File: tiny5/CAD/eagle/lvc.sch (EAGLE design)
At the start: 6 parts, among them U1 LT3007

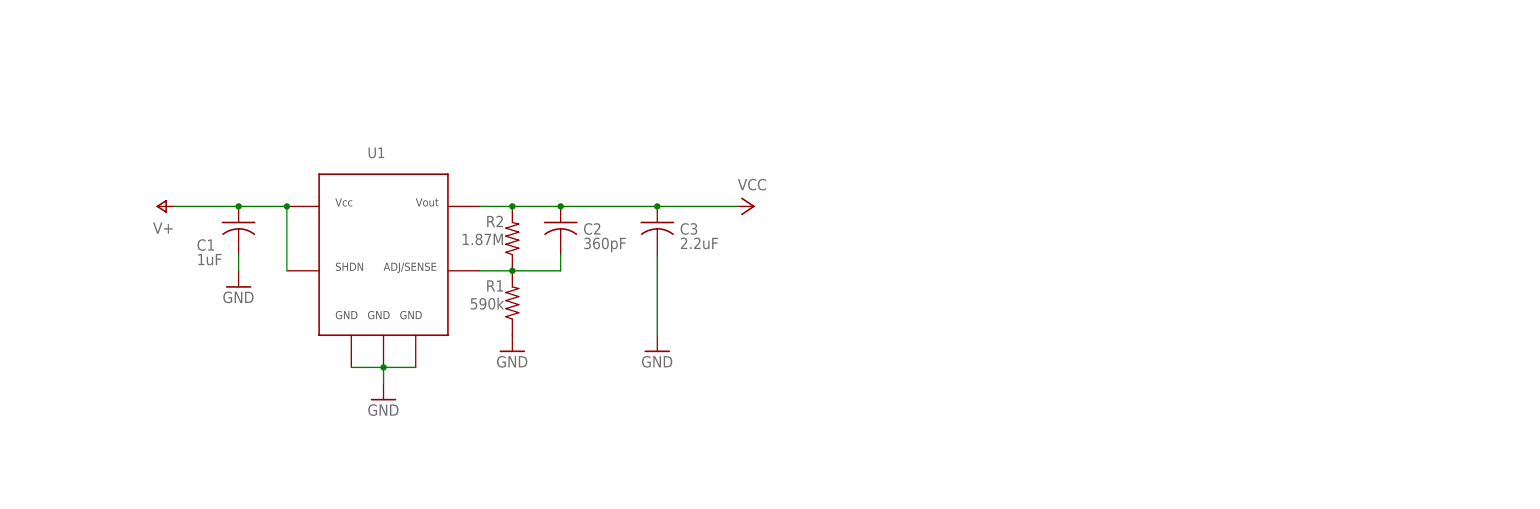
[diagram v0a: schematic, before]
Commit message: added mcu block, updated libraries
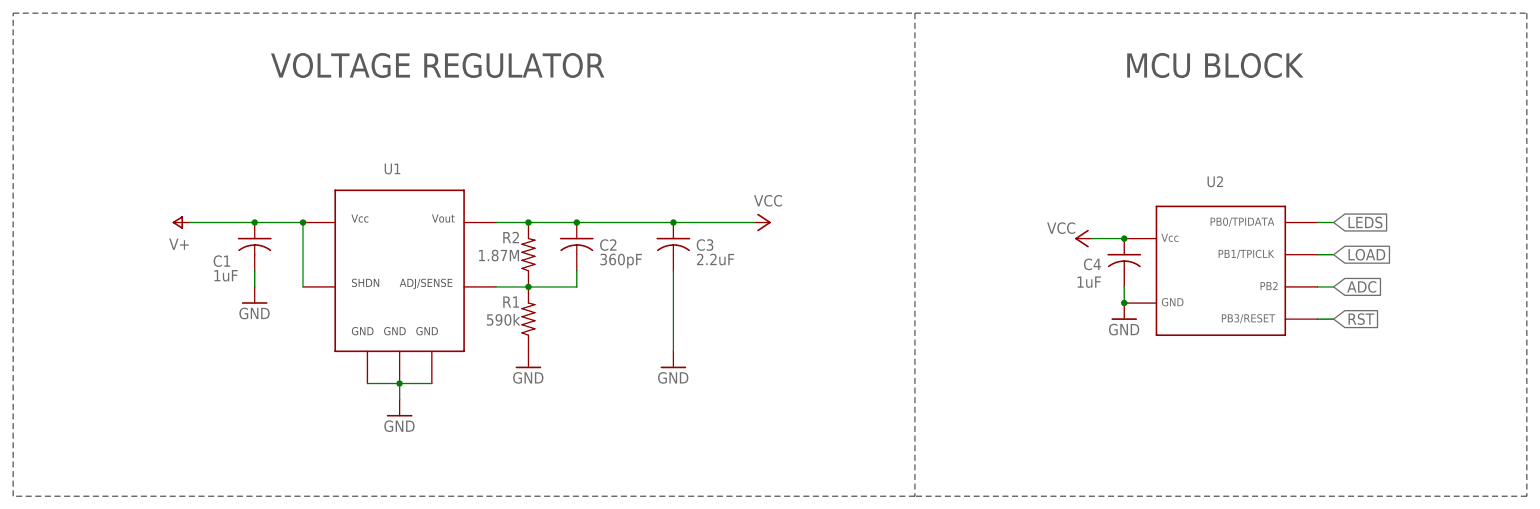
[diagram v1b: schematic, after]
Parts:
- added C4: 1uF, resistor:C-USC0603
- added U2: ATTINY5, AR_mcu:ATTINY5
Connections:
- new net ADC: U2.PB2
- new net LEDS: U2.PB0/TPID
- new net LOAD: U2.PB1/TPICLK
- new net RST: U2.PB3/RST
- net GND: now also C4.2, U2.GND
- net VCC: now also C4.1, U2.VCC
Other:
- note added: "MCU BLOCK"
- note added: "VOLTAGE REGULATOR"
- moved on the sheet: C1, C2, C3, R1, R2, U1

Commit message: Went from adjustable to fixed voltage reg.
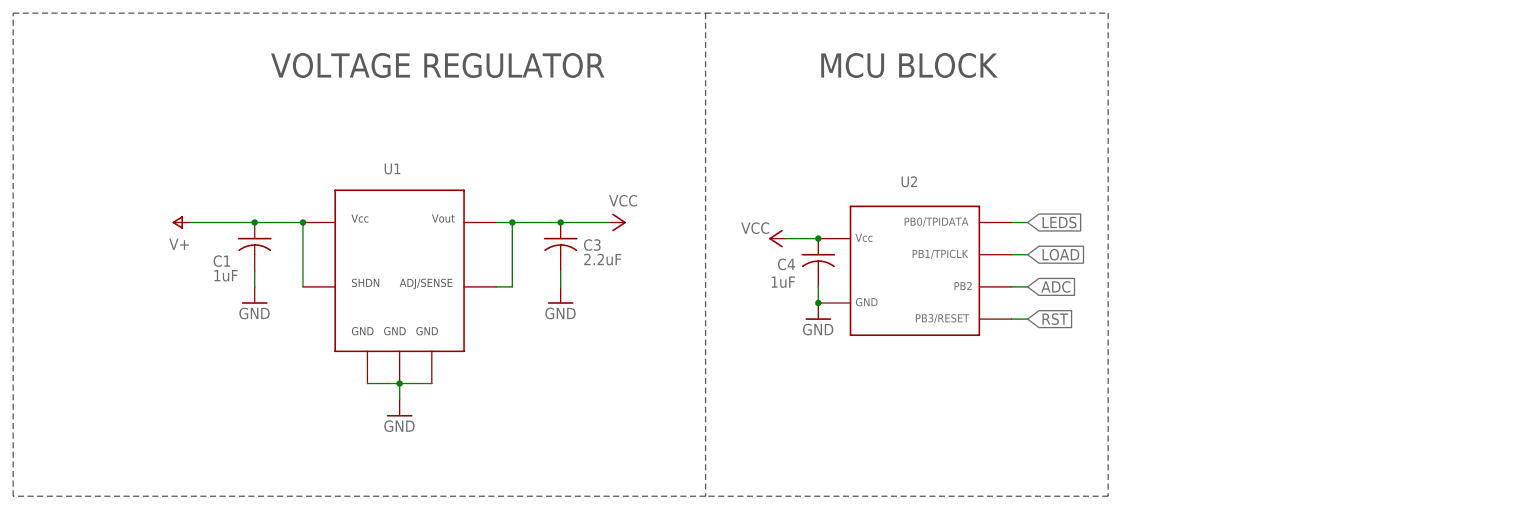
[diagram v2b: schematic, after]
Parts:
- removed C2: 360pF, resistor:C-USC0603
- removed R1: 590k, resistor:R-US_R0603
- removed R2: 1.87M, resistor:R-US_R0603
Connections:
- removed net N$2: C2.2, R1.2, R2.1, U1.ADJ/SENSE
- net GND: no longer R1.1
- net VCC: now also U1.ADJ/SENSE; no longer C2.1, R2.2
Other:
- moved on the sheet: C3, C4, U2
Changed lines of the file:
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@@
 <part name="C1" library="resistor" deviceset="C-US" device="C0603" value="1uF"/>
 <part name="GND2" library="supply1" deviceset="GND" device=""/>
-<part name="R1" library="resistor" deviceset="R-US_" device="R0603" value="590k"/>
-<part name="R2" library="resistor" deviceset="R-US_" device="R0603" value="1.87M"/>
-<part name="GND3" library="supply1" deviceset="GND" device=""/>
 <part name="U1" library="AR_voltage_reg" deviceset="LT3007" device=""/>
-<part name="C2" library="resistor" deviceset="C-US" device="C0603" value="360pF"/>
 <part name="C3" library="resistor" deviceset="C-US" device="C0603" value="2.2uF"/>
 <part name="GND4" library="supply1" deviceset="GND" device=""/>
@@
 <sheet>
 <plain>
-<wire x1="-71.12" y1="99.06" x2="25.4" y2="99.06" width="0.1524" layer="97" style="shortdash"/>
-<wire x1="25.4" y1="99.06" x2="25.4" y2="22.86" width="0.1524" layer="97" style="shortdash"/>
-<wire x1="25.4" y1="22.86" x2="-71.12" y2="22.86" width="0.1524" layer="97" style="shortdash"/>
-<wire x1="-71.12" y1="22.86" x2="-213.36" y2="22.86" width="0.1524" layer="97" style="shortdash"/>
+<wire x1="-104.14" y1="99.06" x2="-40.64" y2="99.06" width="0.1524" layer="97" style="shortdash"/>
+<wire x1="-40.64" y1="99.06" x2="-40.64" y2="22.86" width="0.1524" layer="97" style="shortdash"/>
+<wire x1="-40.64" y1="22.86" x2="-104.14" y2="22.86" width="0.1524" layer="97" style="shortdash"/>
+<wire x1="-104.14" y1="22.86" x2="-213.36" y2="22.86" width="0.1524" layer="97" style="shortdash"/>
 <wire x1="-213.36" y1="22.86" x2="-213.36" y2="99.06" width="0.1524" layer="97" style="shortdash"/>
-<wire x1="-213.36" y1="99.06" x2="-71.12" y2="99.06" width="0.1524" layer="97" style="shortdash"/>
-<wire x1="-71.12" y1="99.06" x2="-71.12" y2="22.86" width="0.1524" layer="97" style="shortdash"/>
+<wire x1="-213.36" y1="99.06" x2="-104.14" y2="99.06" width="0.1524" layer="97" style="shortdash"/>
+<wire x1="-104.14" y1="99.06" x2="-104.14" y2="22.86" width="0.1524" layer="97" style="shortdash"/>
 <text x="-172.72" y="88.9" size="3.81" layer="97">VOLTAGE REGULATOR</text>
-<text x="-38.1" y="88.9" size="3.81" layer="97">MCU BLOCK</text>
+<text x="-86.36" y="88.9" size="3.81" layer="97">MCU BLOCK</text>
 </plain>
 <instances>
@@
 </instance>
 <instance part="GND2" gate="1" x="-175.26" y="53.34"/>
-<instance part="R1" gate="G$1" x="-132.08" y="50.8" smashed="yes" rot="R90">
-<attribute name="NAME" x="-133.35" y="54.3814" size="1.778" layer="95" rot="R180"/>
-<attribute name="VALUE" x="-133.35" y="51.562" size="1.778" layer="96" rot="R180"/>
-</instance>
-<instance part="R2" gate="G$1" x="-132.08" y="60.96" smashed="yes" rot="R90">
-<attribute name="NAME" x="-133.35" y="64.5414" size="1.778" layer="95" rot="R180"/>
-<attribute name="VALUE" x="-133.35" y="61.722" size="1.778" layer="96" rot="R180"/>
-</instance>
-<instance part="GND3" gate="1" x="-132.08" y="43.18"/>
 <instance part="U1" gate="G$1" x="-152.4" y="58.42" smashed="yes">
 <attribute name="NAME" x="-154.94" y="73.66" size="1.6764" layer="95"/>
 </instance>
-<instance part="C2" gate="G$1" x="-124.46" y="63.5" smashed="yes">
-<attribute name="NAME" x="-120.904" y="61.595" size="1.778" layer="95"/>
-<attribute name="VALUE" x="-120.904" y="59.309" size="1.778" layer="96"/>
+<instance part="C3" gate="G$1" x="-127" y="63.5" smashed="yes">
+<attribute name="NAME" x="-123.444" y="61.595" size="1.778" layer="95"/>
+<attribute name="VALUE" x="-123.444" y="59.309" size="1.778" layer="96"/>
 </instance>
-<instance part="C3" gate="G$1" x="-109.22" y="63.5" smashed="yes">
-<attribute name="NAME" x="-105.664" y="61.595" size="1.778" layer="95"/>
-<attribute name="VALUE" x="-105.664" y="59.309" size="1.778" layer="96"/>
+<instance part="GND4" gate="1" x="-127" y="53.34"/>
+<instance part="P+1" gate="VCC" x="-116.84" y="66.04" rot="R270"/>
+<instance part="P+2" gate="1" x="-187.96" y="66.04" rot="R90"/>
+<instance part="P+3" gate="VCC" x="-93.98" y="63.5" smashed="yes" rot="R90">
+<attribute name="VALUE" x="-93.98" y="66.04" size="1.778" layer="96" rot="R180"/>
 </instance>
-<instance part="GND4" gate="1" x="-109.22" y="43.18"/>
-<instance part="P+1" gate="VCC" x="-93.98" y="66.04" rot="R270"/>
-<instance part="P+2" gate="1" x="-187.96" y="66.04" rot="R90"/>
-<instance part="P+3" gate="VCC" x="-45.72" y="63.5" smashed="yes" rot="R90">
-<attribute name="VALUE" x="-45.72" y="66.04" size="1.778" layer="96" rot="R180"/>
+<instance part="C4" gate="G$1" x="-86.36" y="60.96" smashed="yes">
+<attribute name="NAME" x="-89.916" y="60.325" size="1.778" layer="95" rot="R180"/>
+<attribute name="VALUE" x="-89.916" y="57.531" size="1.778" layer="96" rot="R180"/>
 </instance>
-<instance part="C4" gate="G$1" x="-38.1" y="60.96" smashed="yes">
-<attribute name="NAME" x="-41.656" y="60.325" size="1.778" layer="95" rot="R180"/>
-<attribute name="VALUE" x="-41.656" y="57.531" size="1.778" layer="96" rot="R180"/>
-</instance>
-<instance part="GND5" gate="1" x="-38.1" y="50.8"/>
-<instance part="U2" gate="G$1" x="-22.86" y="58.42" smashed="yes">
-<attribute name="NAME" x="-25.146" y="71.628" size="1.6764" layer="95"/>
+<instance part="GND5" gate="1" x="-86.36" y="50.8"/>
+<instance part="U2" gate="G$1" x="-71.12" y="58.42" smashed="yes">
+<attribute name="NAME" x="-73.406" y="71.628" size="1.6764" layer="95"/>
 </instance>
 </instances>
@@
 <pinref part="GND2" gate="1" pin="GND"/>
 <wire x1="-175.26" y1="55.88" x2="-175.26" y2="58.42" width="0.1524" layer="91"/>
-</segment>
-<segment>
-<pinref part="R1" gate="G$1" pin="1"/>
-<pinref part="GND3" gate="1" pin="GND"/>
 </segment>
 <segment>
@@
 <pinref part="C3" gate="G$1" pin="2"/>
 <pinref part="GND4" gate="1" pin="GND"/>
-<wire x1="-109.22" y1="45.72" x2="-109.22" y2="58.42" width="0.1524" layer="91"/>
+<wire x1="-127" y1="55.88" x2="-127" y2="58.42" width="0.1524" layer="91"/>
 </segment>
 <segment>
 <pinref part="GND5" gate="1" pin="GND"/>
-<pinref part="GND5" gate="1" pin="GND"/>
 <pinref part="U2" gate="G$1" pin="GND"/>
 <pinref part="C4" gate="G$1" pin="2"/>
-<wire x1="-38.1" y1="53.34" x2="-38.1" y2="55.88" width="0.1524" layer="91"/>
-<junction x="-38.1" y="53.34"/>
-</segment>
-</net>
-<net name="N$2" class="0">
-<segment>
-<pinref part="R1" gate="G$1" pin="2"/>
-<pinref part="R2" gate="G$1" pin="1"/>
-<wire x1="-137.16" y1="55.88" x2="-132.08" y2="55.88" width="0.1524" layer="91"/>
-<junction x="-132.08" y="55.88"/>
-<pinref part="U1" gate="G$1" pin="ADJ/SENSE"/>
-<pinref part="C2" gate="G$1" pin="2"/>
-<wire x1="-124.46" y1="58.42" x2="-124.46" y2="55.88" width="0.1524" layer="91"/>
-<wire x1="-124.46" y1="55.88" x2="-132.08" y2="55.88" width="0.1524" layer="91"/>
+<wire x1="-86.36" y1="53.34" x2="-86.36" y2="55.88" width="0.1524" layer="91"/>
+<junction x="-86.36" y="53.34"/>
 </segment>
 </net>
@@
 <net name="VCC" class="0">
 <segment>
-<pinref part="R2" gate="G$1" pin="2"/>
-<wire x1="-137.16" y1="66.04" x2="-132.08" y2="66.04" width="0.1524" layer="91"/>
 <pinref part="U1" gate="G$1" pin="OUT"/>
-<pinref part="C2" gate="G$1" pin="1"/>
-<wire x1="-132.08" y1="66.04" x2="-124.46" y2="66.04" width="0.1524" layer="91"/>
-<junction x="-132.08" y="66.04"/>
 <pinref part="C3" gate="G$1" pin="1"/>
-<wire x1="-124.46" y1="66.04" x2="-109.22" y2="66.04" width="0.1524" layer="91"/>
-<junction x="-124.46" y="66.04"/>
+<wire x1="-137.16" y1="66.04" x2="-134.62" y2="66.04" width="0.1524" layer="91"/>
 <pinref part="P+1" gate="VCC" pin="VCC"/>
-<wire x1="-96.52" y1="66.04" x2="-109.22" y2="66.04" width="0.1524" layer="91"/>
-<junction x="-109.22" y="66.04"/>
+<wire x1="-134.62" y1="66.04" x2="-127" y2="66.04" width="0.1524" layer="91"/>
+<wire x1="-119.38" y1="66.04" x2="-127" y2="66.04" width="0.1524" layer="91"/>
+<junction x="-127" y="66.04"/>
+<pinref part="U1" gate="G$1" pin="ADJ/SENSE"/>
+<wire x1="-137.16" y1="55.88" x2="-134.62" y2="55.88" width="0.1524" layer="91"/>
+<wire x1="-134.62" y1="55.88" x2="-134.62" y2="66.04" width="0.1524" layer="91"/>
+<junction x="-134.62" y="66.04"/>
 </segment>
 <segment>
 <pinref part="P+3" gate="VCC" pin="VCC"/>
-<wire x1="-43.18" y1="63.5" x2="-38.1" y2="63.5" width="0.1524" layer="91"/>
+<wire x1="-91.44" y1="63.5" x2="-86.36" y2="63.5" width="0.1524" layer="91"/>
 <pinref part="C4" gate="G$1" pin="1"/>
 <pinref part="U2" gate="G$1" pin="VCC"/>
-<junction x="-38.1" y="63.5"/>
+<junction x="-86.36" y="63.5"/>
 </segment>
 </net>
@@
 <segment>
 <pinref part="U2" gate="G$1" pin="PB0/TPID"/>
-<wire x1="-7.62" y1="66.04" x2="-5.08" y2="66.04" width="0.1524" layer="91"/>
-<label x="-5.08" y="66.04" size="1.778" layer="95" xref="yes"/>
+<wire x1="-55.88" y1="66.04" x2="-53.34" y2="66.04" width="0.1524" layer="91"/>
+<label x="-53.34" y="66.04" size="1.778" layer="95" xref="yes"/>
 </segment>
 </net>
@@
 <segment>
 <pinref part="U2" gate="G$1" pin="PB1/TPICLK"/>
-<wire x1="-7.62" y1="60.96" x2="-5.08" y2="60.96" width="0.1524" layer="91"/>
-<label x="-5.08" y="60.96" size="1.778" layer="95" xref="yes"/>
+<wire x1="-55.88" y1="60.96" x2="-53.34" y2="60.96" width="0.1524" layer="91"/>
+<label x="-53.34" y="60.96" size="1.778" layer="95" xref="yes"/>
 </segment>
 </net>
@@
 <segment>
 <pinref part="U2" gate="G$1" pin="PB2"/>
-<wire x1="-7.62" y1="55.88" x2="-5.08" y2="55.88" width="0.1524" layer="91"/>
-<label x="-5.08" y="55.88" size="1.778" layer="95" xref="yes"/>
+<wire x1="-55.88" y1="55.88" x2="-53.34" y2="55.88" width="0.1524" layer="91"/>
+<label x="-53.34" y="55.88" size="1.778" layer="95" xref="yes"/>
 </segment>
 </net>
@@
 <segment>
 <pinref part="U2" gate="G$1" pin="PB3/RST"/>
-<wire x1="-7.62" y1="50.8" x2="-5.08" y2="50.8" width="0.1524" layer="91"/>
-<label x="-5.08" y="50.8" size="1.778" layer="95" xref="yes"/>
+<wire x1="-55.88" y1="50.8" x2="-53.34" y2="50.8" width="0.1524" layer="91"/>
+<label x="-53.34" y="50.8" size="1.778" layer="95" xref="yes"/>
 </segment>
 </net>

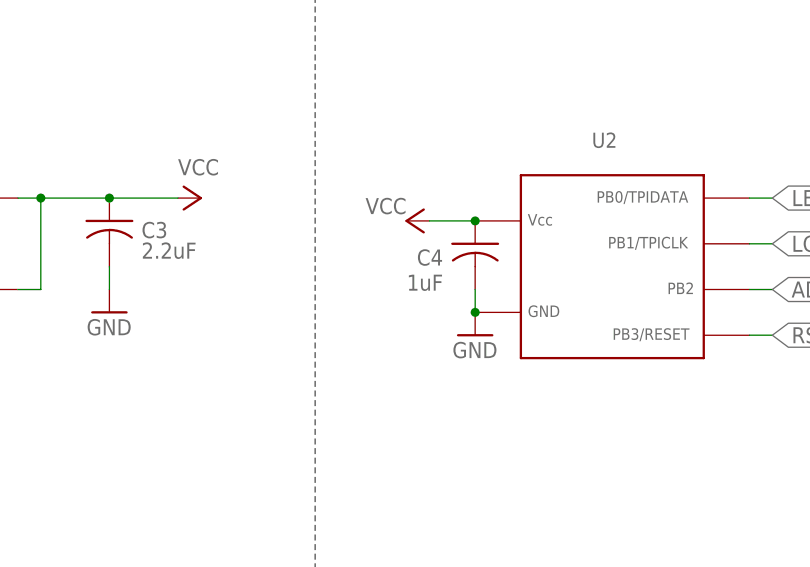
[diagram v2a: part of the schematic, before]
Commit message: Added op amp
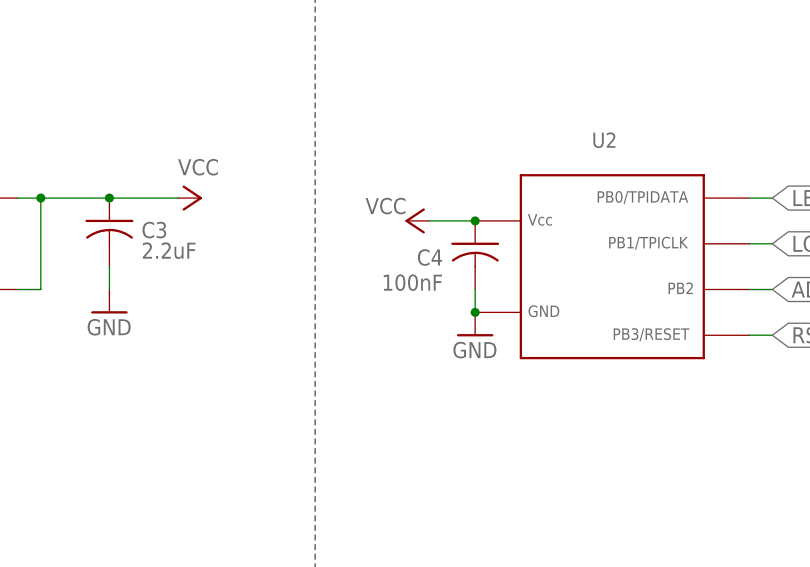
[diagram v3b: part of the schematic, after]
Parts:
- C4: value 1uF -> 100nF
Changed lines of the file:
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@@
 <part name="P+2" library="supply1" deviceset="V+" device=""/>
 <part name="P+3" library="supply1" deviceset="VCC" device=""/>
-<part name="C4" library="resistor" deviceset="C-US" device="C0603" value="1uF"/>
+<part name="C4" library="resistor" deviceset="C-US" device="C0603" value="100nF"/>
 <part name="GND5" library="supply1" deviceset="GND" device=""/>
 <part name="U2" library="AR_mcu" deviceset="ATTINY5" device=""/>

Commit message: Prettified MOSFET symbols
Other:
- moved on the sheet: C1, C3, C4, U1, U2
